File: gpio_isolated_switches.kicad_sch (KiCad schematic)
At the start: 38 parts, among them J1 Conn_01x02, J2 Conn_01x02, J3 Conn_01x02, J4 Conn_01x02, J5 SBC GPIO, J6 Conn_01x02, Q1 BUK7M10-40EX, Q2 BUK7M10-40EX, Q3 BUK7M10-40EX, Q4 BUK7M10-40EX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

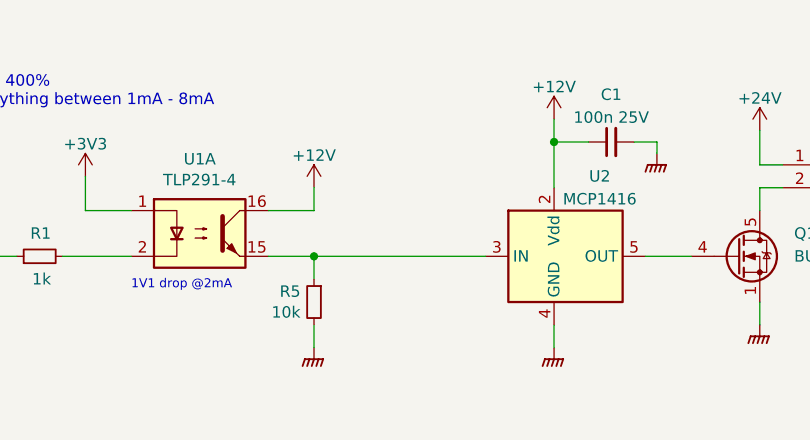
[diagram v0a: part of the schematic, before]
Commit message: Adding SW0 direct output from optocoupler
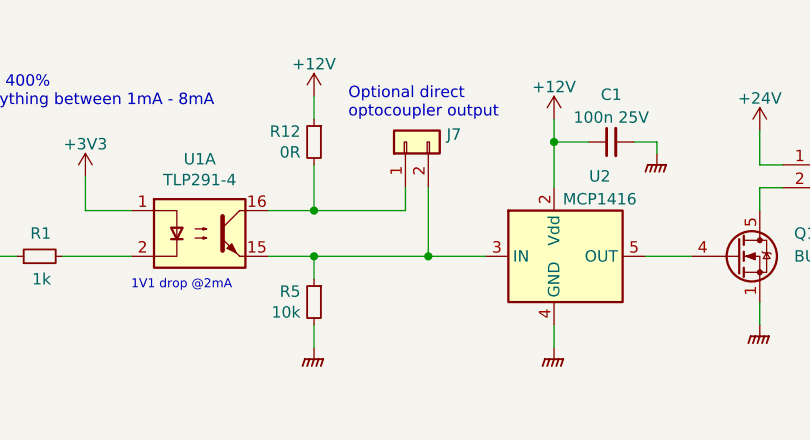
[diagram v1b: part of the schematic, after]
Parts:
- added J7: Conn_01x02, Connector_PinHeader_2.54mm:PinHeader_1x02_P2.54mm_Vertical, symbol Connector_Generic:Conn_01x02
- added R12: 0R, Resistor_SMD:R_0603_1608Metric, symbol Device:R_Small
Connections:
- net +12V: now also R12.1; no longer U1.16
- net at R5.1, U1.15, U2.3 (IN): now also J7.2 (Pin_2)
- new net: J7.1 (Pin_1), R12.2, U1.16
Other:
- note added: "Optional direct optocoupler output"
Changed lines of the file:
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@@
   (junction (at 214.63 29.21) (diameter 0) (color 0 0 0 0)
   )
+  (junction (at 76.2 39.37) (diameter 0) (color 0 0 0 0)
+  )
   (junction (at 63.5 39.37) (diameter 0) (color 0 0 0 0)
   )
   (junction (at 90.17 73.66) (diameter 0) (color 0 0 0 0)
   )
+  (junction (at 63.5 34.29) (diameter 0) (color 0 0 0 0)
+  )
   (junction (at 180.34 29.21) (diameter 0) (color 0 0 0 0)
   )
@@
   (junction (at 264.16 63.5) (diameter 0) (color 0 0 0 0)
   )
+  (wire (pts (xy 76.2 31.75) (xy 76.2 39.37))
+    (stroke (width 0) (type default) (color 0 0 0 0))
+  )
   (wire (pts (xy 63.5 41.91) (xy 63.5 39.37))
     (stroke (width 0) (type default) (color 0 0 0 0))
@@
     (stroke (width 0) (type default) (color 0 0 0 0))
   )
-  (wire (pts (xy 63.5 39.37) (xy 82.55 39.37))
+  (wire (pts (xy 63.5 39.37) (xy 76.2 39.37))
     (stroke (width 0) (type default) (color 0 0 0 0))
   )
@@
     (stroke (width 0) (type default) (color 0 0 0 0))
   )
+  (wire (pts (xy 63.5 34.29) (xy 73.66 34.29))
+    (stroke (width 0) (type default) (color 0 0 0 0))
+  )
   (wire (pts (xy 90.17 71.12) (xy 90.17 73.66))
     (stroke (width 0) (type default) (color 0 0 0 0))
@@
     (stroke (width 0) (type default) (color 0 0 0 0))
   )
+  (wire (pts (xy 76.2 39.37) (xy 82.55 39.37))
+    (stroke (width 0) (type default) (color 0 0 0 0))
+  )
   (wire (pts (xy 105.41 173.99) (xy 100.33 173.99))
     (stroke (width 0) (type default) (color 0 0 0 0))
   )
-  (wire (pts (xy 63.5 31.75) (xy 63.5 34.29))
+  (wire (pts (xy 63.5 21.59) (xy 63.5 24.13))
     (stroke (width 0) (type default) (color 0 0 0 0))
   )
@@
     (stroke (width 0) (type default) (color 0 0 0 0))
   )
+  (wire (pts (xy 73.66 31.75) (xy 73.66 34.29))
+    (stroke (width 0) (type default) (color 0 0 0 0))
+  )
   (wire (pts (xy 113.03 160.02) (xy 113.03 163.83))
     (stroke (width 0) (type default) (color 0 0 0 0))
@@
     (stroke (width 0) (type default) (color 0 0 0 0))
   )
+  (wire (pts (xy 63.5 29.21) (xy 63.5 34.29))
+    (stroke (width 0) (type default) (color 0 0 0 0))
+  )
   (wire (pts (xy 113.03 91.44) (xy 113.03 93.98))
     (stroke (width 0) (type default) (color 0 0 0 0))
@@
     (effects (font (size 1.27 1.27)) (justify right bottom))
   )
+  (text "Optional direct\noptocoupler output" (at 67.31 24.13 0)
+    (effects (font (size 1.27 1.27)) (justify left bottom))
+  )
   (text "Also fits BAT54, BAT54S" (at 256.54 96.52 0)
     (effects (font (size 1.27 1.27)) (justify left bottom))
@@
     (pin "2")
   )
+  (symbol (lib_id "Device:R_Small") (at 63.5 26.67 0) (mirror y) (unit 1)
+    (in_bom yes) (on_board yes)
+    (property "Reference" "R12" (id 0) (at 62.0014 25.5016 0)
+      (effects (font (size 1.27 1.27)) (justify left))
+    )
+    (property "Value" "0R" (id 1) (at 62.0014 27.813 0)
+      (effects (font (size 1.27 1.27)) (justify left))
+    )
+    (property "Footprint" "Resistor_SMD:R_0603_1608Metric" (id 2) (at 63.5 26.67 0)
+      (effects (font (size 1.27 1.27)) hide)
+    )
+    (property "Datasheet" "~" (id 3) (at 63.5 26.67 0)
+      (effects (font (size 1.27 1.27)) hide)
+    )
+    (pin "1")
+    (pin "2")
+  )
   (symbol (lib_id "Device:R_Small") (at 205.74 44.45 180) (unit 1)
     (in_bom yes) (on_board yes)
@@
     (pin "5")
   )
-  (symbol (lib_id "power:+12V") (at 63.5 31.75 0) (unit 1)
+  (symbol (lib_id "power:+12V") (at 63.5 21.59 0) (unit 1)
     (in_bom yes) (on_board yes) (fields_autoplaced)
-    (property "Reference" "#PWR0109" (id 0) (at 63.5 35.56 0)
+    (property "Reference" "#PWR0109" (id 0) (at 63.5 25.4 0)
       (effects (font (size 1.27 1.27)) hide)
     )
-    (property "Value" "+12V" (id 1) (at 63.5 28.1742 0))
-    (property "Footprint" "" (id 2) (at 63.5 31.75 0)
+    (property "Value" "+12V" (id 1) (at 63.5 18.0142 0))
+    (property "Footprint" "" (id 2) (at 63.5 21.59 0)
       (effects (font (size 1.27 1.27)) hide)
     )
-    (property "Datasheet" "" (id 3) (at 63.5 31.75 0)
+    (property "Datasheet" "" (id 3) (at 63.5 21.59 0)
       (effects (font (size 1.27 1.27)) hide)
     )
     (pin "1")
   )
+  (symbol (lib_id "Connector_Generic:Conn_01x02") (at 73.66 26.67 90) (unit 1)
+    (in_bom yes) (on_board yes) (fields_autoplaced)
+    (property "Reference" "J7" (id 0) (at 78.232 25.8353 90)
+      (effects (font (size 1.27 1.27)) (justify right))
+    )
+    (property "Value" "Conn_01x02" (id 1) (at 78.232 28.3722 90)
+      (effects (font (size 1.27 1.27)) (justify right) hide)
+    )
+    (property "Footprint" "Connector_PinHeader_2.54mm:PinHeader_1x02_P2.54mm_Vertical" (id 2) (at 73.66 26.67 0)
+      (effects (font (size 1.27 1.27)) hide)
+    )
+    (property "Datasheet" "~" (id 3) (at 73.66 26.67 0)
+      (effects (font (size 1.27 1.27)) hide)
+    )
+    (pin "1")
+    (pin "2")
+  )
   (symbol (lib_id "power:+3V3") (at 38.1 30.48 0) (unit 1)
     (in_bom yes) (on_board yes) (fields_autoplaced)
@@
       (reference "J6") (unit 1) (value "Conn_01x02") (footprint "TerminalBlock:TerminalBlock_Altech_AK300-2_P5.00mm")
     )
+    (path "/8146df08-13ce-426a-89d1-054ea15606e2"
+      (reference "J7") (unit 1) (value "Conn_01x02") (footprint "Connector_PinHeader_2.54mm:PinHeader_1x02_P2.54mm_Vertical")
+    )
     (path "/f3baf8c3-0789-441f-a725-2aaec7c0c755"
       (reference "LOGO1") (unit 1) (value "Logo_Open_Hardware_Small") (footprint "Symbol:OSHW-Logo2_9.8x8mm_SilkScreen")
@@
       (reference "R11") (unit 1) (value "100R") (footprint "Resistor_SMD:R_0603_1608Metric")
     )
+    (path "/16b93a35-7de1-4e75-abb4-2b863c4e4bc7"
+      (reference "R12") (unit 1) (value "0R") (footprint "Resistor_SMD:R_0603_1608Metric")
+    )
     (path "/e1989386-dbef-43bb-86bc-5e8b2f58c248"

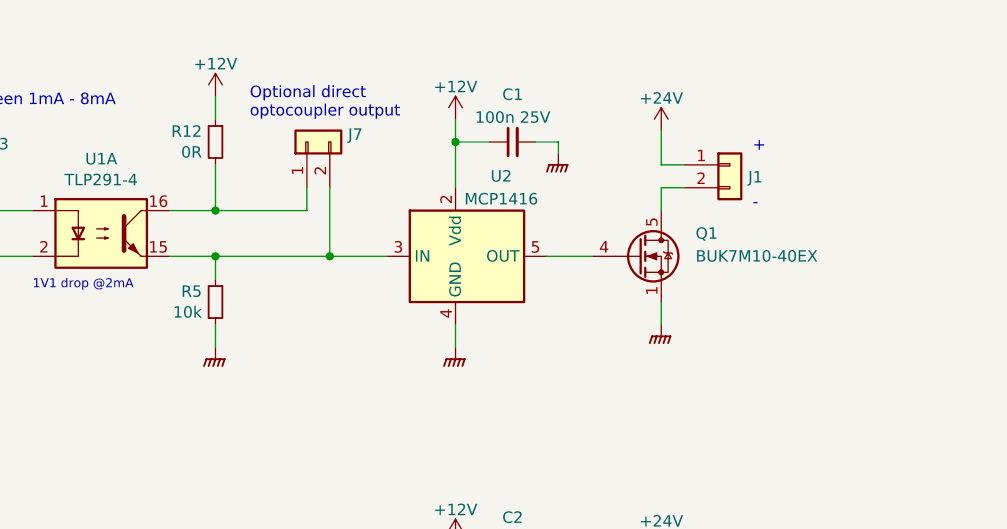
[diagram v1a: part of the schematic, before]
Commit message: Removed SW0 switch, left direct optocoupler output only
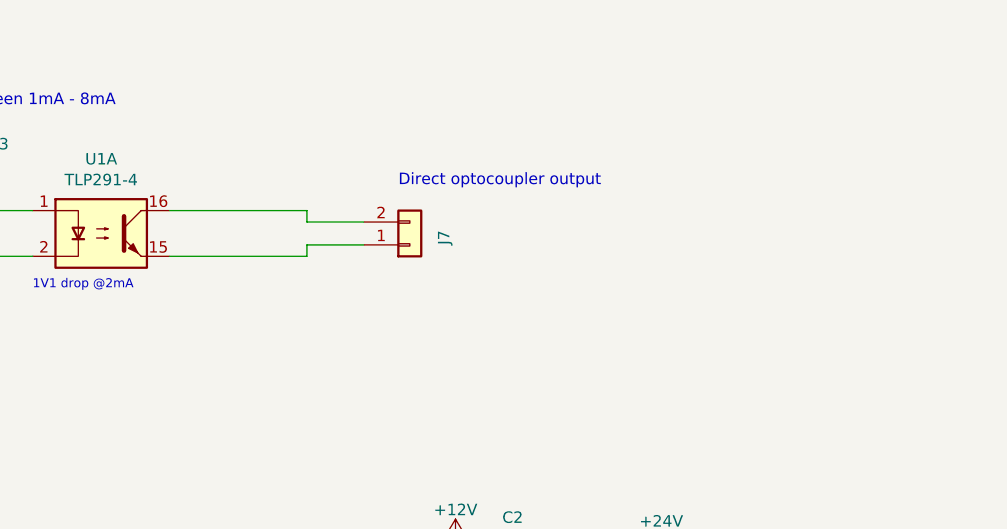
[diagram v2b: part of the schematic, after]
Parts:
- removed C1: 100n 25V, Capacitor_SMD:C_0603_1608Metric, symbol Device:C_Small
- removed J1: Conn_01x02, TerminalBlock:TerminalBlock_Altech_AK300-2_P5.00mm, symbol Connector_Generic:Conn_01x02
- removed Q1: BUK7M10-40EX, Package_TO_SOT_SMD:LFPAK33, symbol Transistor_FET:BUK7M10-40EX
- removed R12: 0R, Resistor_SMD:R_0603_1608Metric, symbol Device:R_Small
- removed R5: 10k, Resistor_SMD:R_0603_1608Metric, symbol Device:R_Small
- removed U2: MCP1416, Package_TO_SOT_SMD:SOT-23-5, symbol Driver_FET:MCP1416
- J7: footprint Connector_PinHeader_2.54mm:PinHeader_1x02_P2.54mm_Vertical -> Connector_PinHeader_2.54mm:PinHeader_1x02_P2.54mm_Horizontal
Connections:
- net at J7.1 (Pin_1): now also U1.15; no longer U1.16
- net at J7.2 (Pin_2): now also U1.16; no longer U1.15
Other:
- note added: "Direct optocoupler output"
- note removed: "Optional direct optocoupler output"
- moved on the sheet: J7
